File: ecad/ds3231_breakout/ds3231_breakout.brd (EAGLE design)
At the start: 26.2 x 23 mm, 7 parts, among them IC1 DS3231, J1 PTH RA MALE

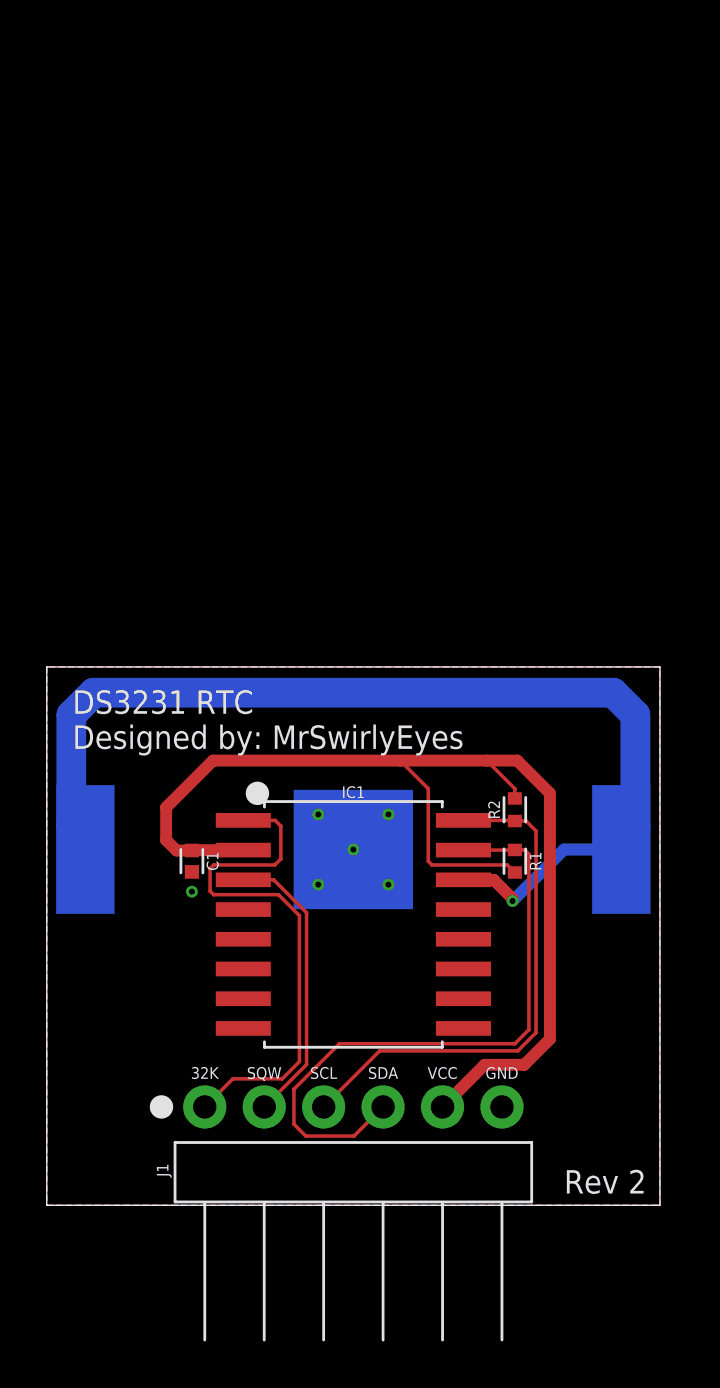
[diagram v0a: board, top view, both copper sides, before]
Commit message: Create DS3231 breakout vesion.  Updated libraries.
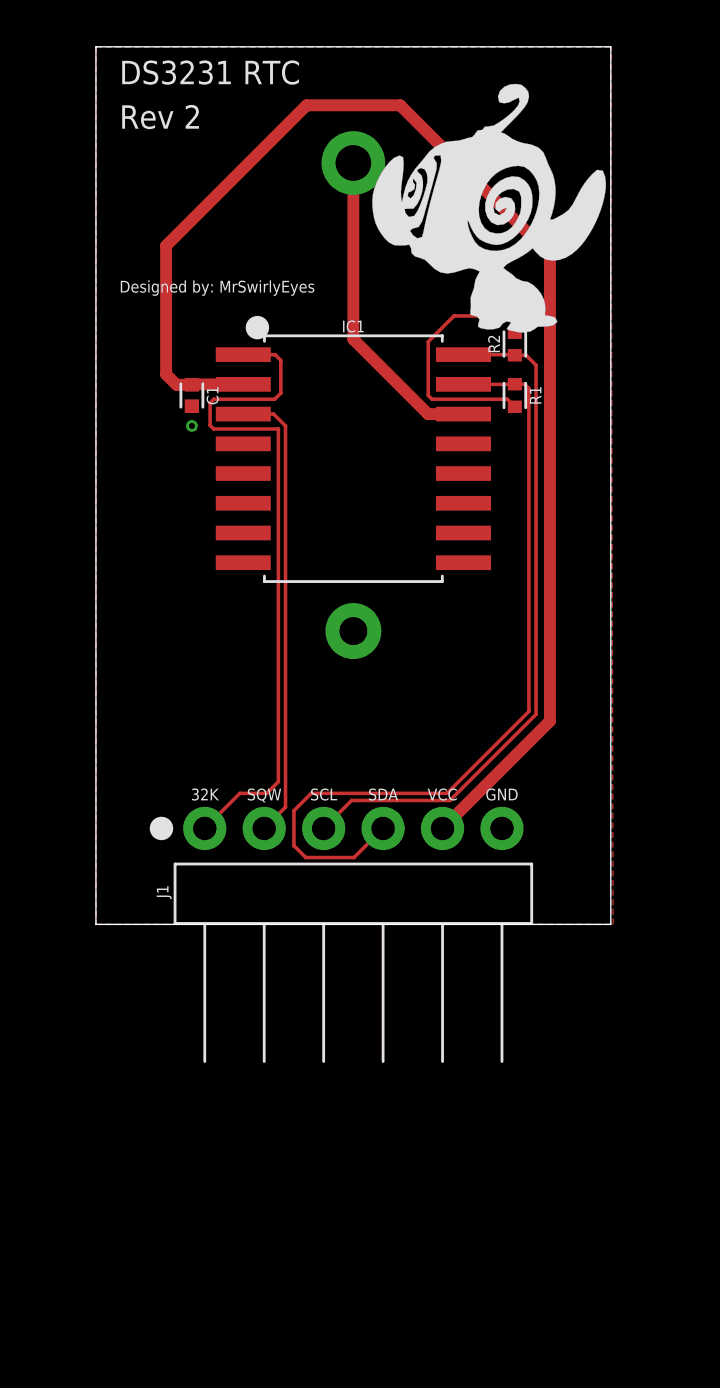
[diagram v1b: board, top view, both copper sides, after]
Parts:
- BATT1: device _batteries:CR-2032 -> _batteries:BATTERY_COINCELL-20MM-PTH
- moved U$1 32.1 mm to (5.80, 30.6), flipped to the top
- moved C1 19.9 mm to (-6.90, 22.6)
- moved R1 19.9 mm to (6.90, 22.6)
- moved IC1 19.9 mm to (0.00, 19.9)
- moved R2 19.9 mm to (6.90, 24.8)
- moved BATT1 16.8 mm to (0.00, 20.0), turned to 0 degrees
- moved J1 11.9 mm to (0.00, 4.10)
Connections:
- net 3V: now also BATT1.+; no longer BATT1.+_1, BATT1.+_2
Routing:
- net 3V: track 45.0 -> 13.6 mm, vias 1 -> 0
- net VCC: track 49.8 -> 69.8 mm
- net SQW: track 12.3 -> 19.6 mm
- net SDA: track 27.5 -> 34.5 mm
- net SCL: track 22.3 -> 29.3 mm
- net 32K: track 22.6 -> 29.3 mm
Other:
- board size 26.2 x 23 mm -> 22 x 37.5 mm
